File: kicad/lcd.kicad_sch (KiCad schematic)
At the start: 2 parts, among them J8 R61529 LCD

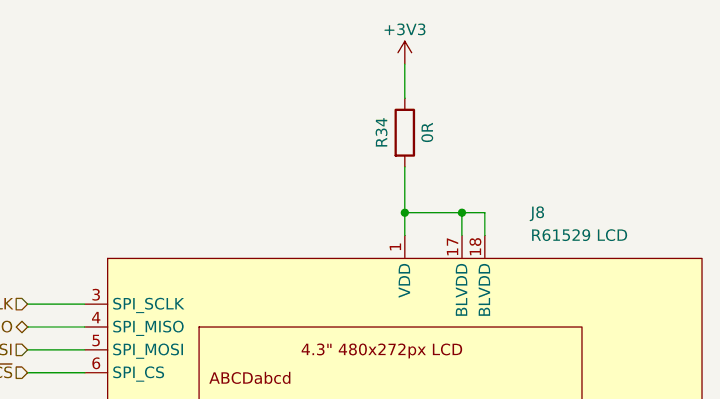
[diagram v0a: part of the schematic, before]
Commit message: remove Rx with 0 Ohms
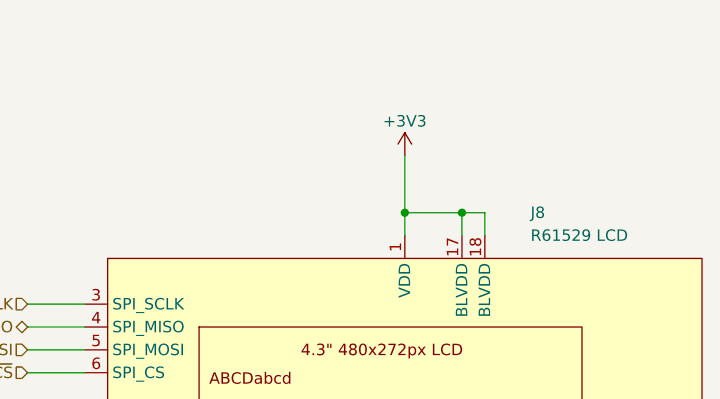
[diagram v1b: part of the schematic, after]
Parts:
- removed R34: 0R, Resistor_SMD:R_0603_1608Metric, symbol Device:R
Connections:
- net +3V3: now also J8.1 (VDD), J8.17 (BLVDD), J8.18 (BLVDD)
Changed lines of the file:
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@@
-    (stroke (width 0) (type default) (color 0 0 0 0))
-  )
-  (wire (pts (xy 137.16 66.04) (xy 137.16 71.12))
     (stroke (width 0) (type default) (color 0 0 0 0))
   )
@@
     (stroke (width 0) (type default) (color 0 0 0 0))
   )
-  (wire (pts (xy 137.16 54.61) (xy 137.16 58.42))
+  (wire (pts (xy 137.16 64.77) (xy 137.16 71.12))
     (stroke (width 0) (type default) (color 0 0 0 0))
   )
@@
     (pin "1")
   )
-  (symbol (lib_id "power:+3V3") (at 137.16 54.61 0) (unit 1)
+  (symbol (lib_id "power:+3V3") (at 137.16 64.77 0) (unit 1)
     (in_bom yes) (on_board yes)
-    (property "Reference" "#PWR056" (id 0) (at 137.16 58.42 0)
+    (property "Reference" "#PWR056" (id 0) (at 137.16 68.58 0)
       (effects (font (size 1.27 1.27)) hide)
     )
-    (property "Value" "+3V3" (id 1) (at 137.16 50.8 0))
-    (property "Footprint" "" (id 2) (at 137.16 54.61 0)
+    (property "Value" "+3V3" (id 1) (at 137.16 60.96 0))
+    (property "Footprint" "" (id 2) (at 137.16 64.77 0)
       (effects (font (size 1.27 1.27)) hide)
     )
-    (property "Datasheet" "" (id 3) (at 137.16 54.61 0)
+    (property "Datasheet" "" (id 3) (at 137.16 64.77 0)
       (effects (font (size 1.27 1.27)) hide)
     )
@@
     (pin "1")
   )
-  (symbol (lib_id "Device:R") (at 137.16 62.23 0) (unit 1)
-    (in_bom yes) (on_board yes)
-    (property "Reference" "R34" (id 0) (at 134.62 62.23 90))
-    (property "Value" "0R" (id 1) (at 139.7 62.23 90))
-    (property "Footprint" "Resistor_SMD:R_0603_1608Metric" (id 2) (at 135.382 62.23 90)
-      (effects (font (size 1.27 1.27)) hide)
-    )
-    (property "Datasheet" "~" (id 3) (at 137.16 62.23 0)
-      (effects (font (size 1.27 1.27)) hide)
-    )
-    (property "Digikey" "541-0.0SBCT-ND" (id 4) (at 137.16 62.23 0)
-      (effects (font (size 1.27 1.27)) hide)
-    )
-    (pin "1")
-    (pin "2")
-  )
 )
